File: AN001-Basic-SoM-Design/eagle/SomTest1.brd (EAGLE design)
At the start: 31.1 x 85 mm, 42 parts, among them U1 MAX17043, U2 BQ24195, U3 XCL223

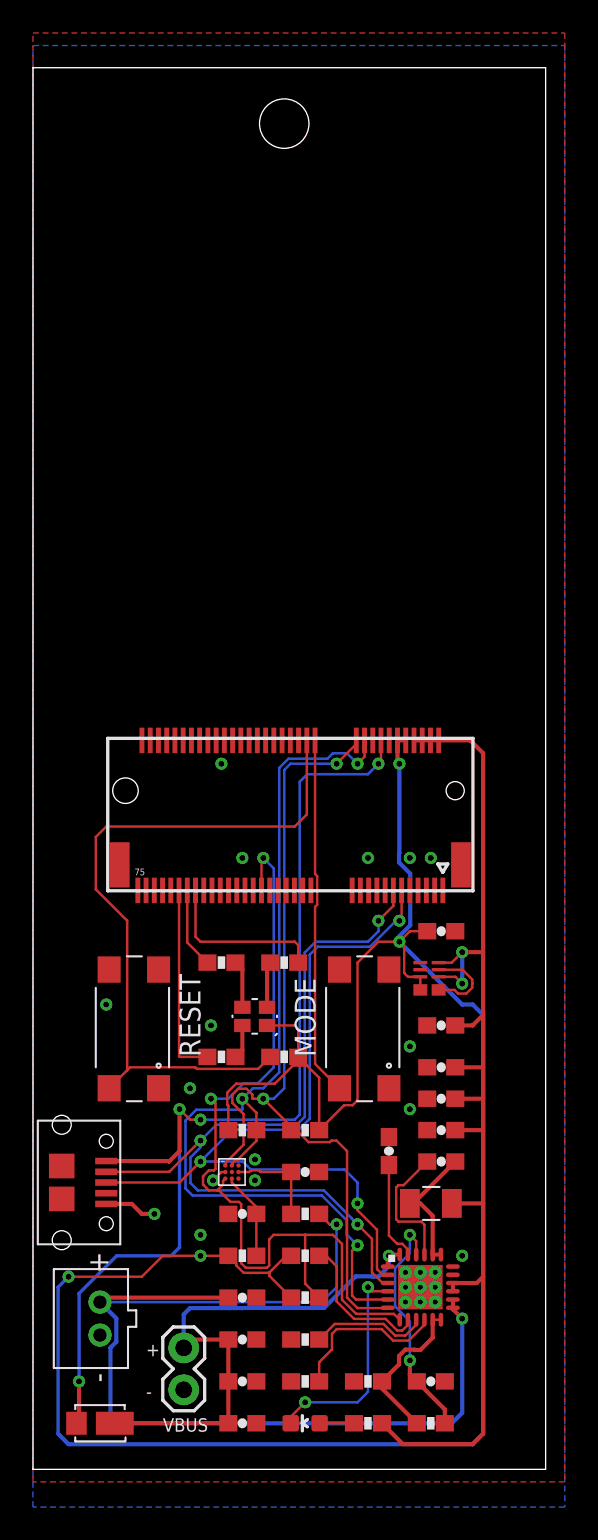
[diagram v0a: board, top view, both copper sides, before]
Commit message: Update M.2 standoff
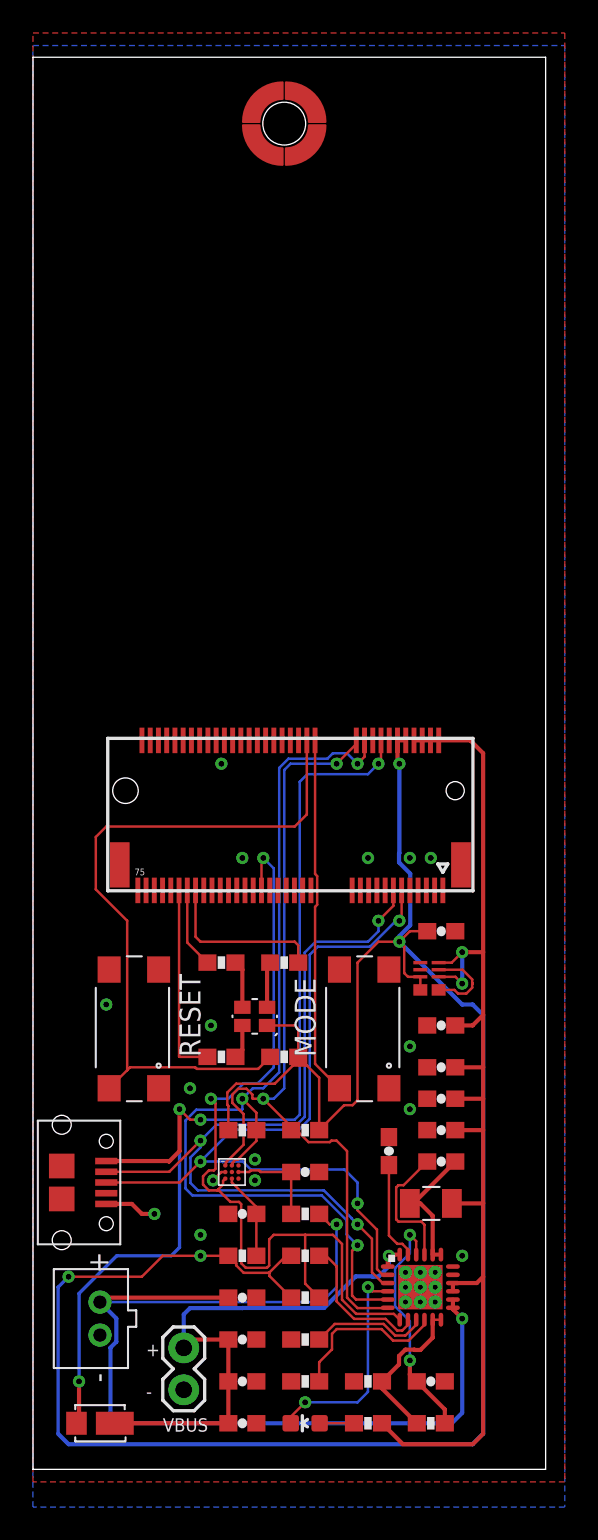
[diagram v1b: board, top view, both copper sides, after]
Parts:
- added U$1: M2-STANDOFF, rickk2:M2-STANDOFF
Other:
- board size 31.1 x 85 mm -> 31.1 x 85.6 mm
- board text added: "SomTest1 v4"
- board text removed: "SomTest1 v3"
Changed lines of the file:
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@@
 <plain>
 <wire x1="0" y1="-0.254" x2="31.095" y2="-0.254" width="0" layer="20"/>
-<wire x1="31.095" y1="-0.254" x2="31.095" y2="84.76" width="0" layer="20"/>
-<wire x1="31.095" y1="84.76" x2="0" y2="84.76" width="0" layer="20"/>
-<wire x1="0" y1="84.76" x2="0" y2="-0.254" width="0" layer="20"/>
+<wire x1="31.095" y1="-0.254" x2="31.095" y2="85.395" width="0" layer="20"/>
+<wire x1="31.095" y1="85.395" x2="0" y2="85.395" width="0" layer="20"/>
+<wire x1="0" y1="85.395" x2="0" y2="-0.254" width="0" layer="20"/>
 <text x="10.16" y="24.765" size="1.27" layer="21" rot="R90">RESET</text>
 <text x="17.145" y="24.765" size="1.27" layer="21" rot="R90">MODE</text>
 <text x="19.05" y="46.99" size="1.27" layer="22" rot="MR0">SomTest1
-v3</text>
-<hole x="15.24" y="81.37" drill="3"/>
+v4</text>
 <text x="6.858" y="6.604" size="0.8128" layer="21">+</text>
 <text x="6.858" y="4.064" size="0.8128" layer="21">-</text>
@@
 </element>
 <element name="JP1" library="rickk2" package="1X02" value="M02PTH" x="9.144" y="7.112" smashed="yes" rot="R270"/>
+<element name="U$1" library="rickk2" package="M2-STANDOFF" value="M2-STANDOFF" x="15.24" y="81.37" smashed="yes"/>
 </elements>
 <signals>
